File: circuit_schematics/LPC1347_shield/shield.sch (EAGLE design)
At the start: 1 part, among them IC1 7805TV

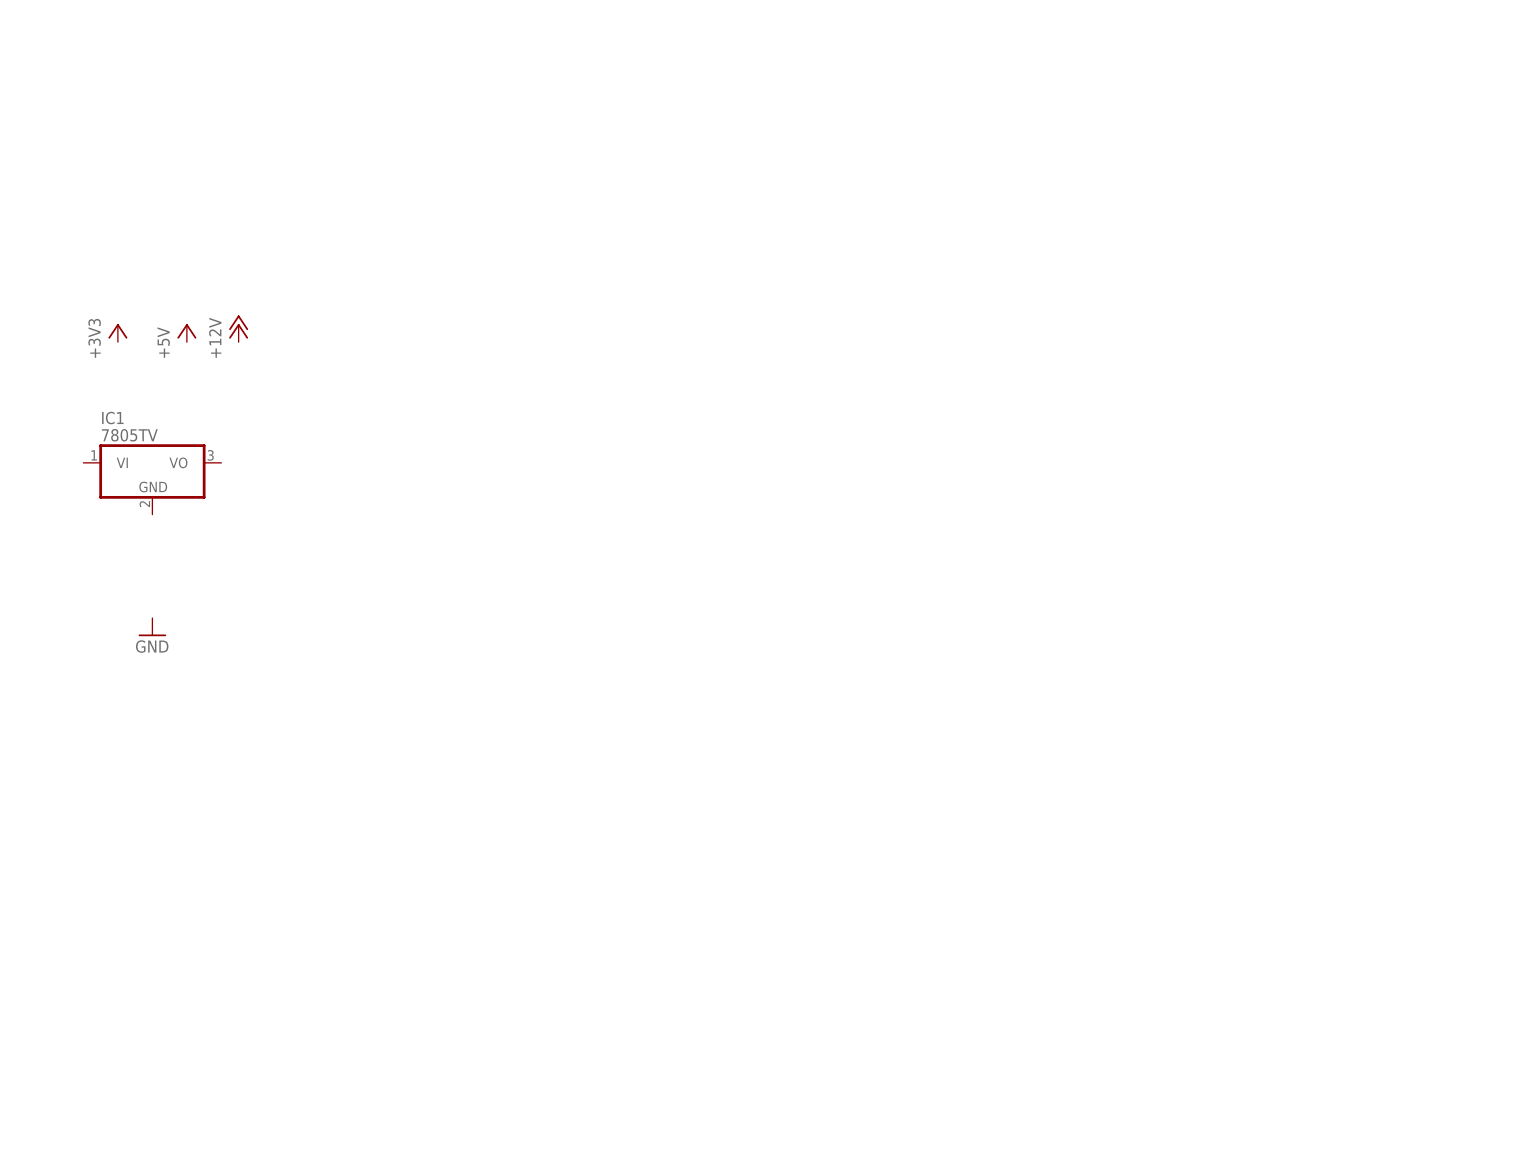
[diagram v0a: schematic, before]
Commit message: Finished circuit board with all traces on top layer.
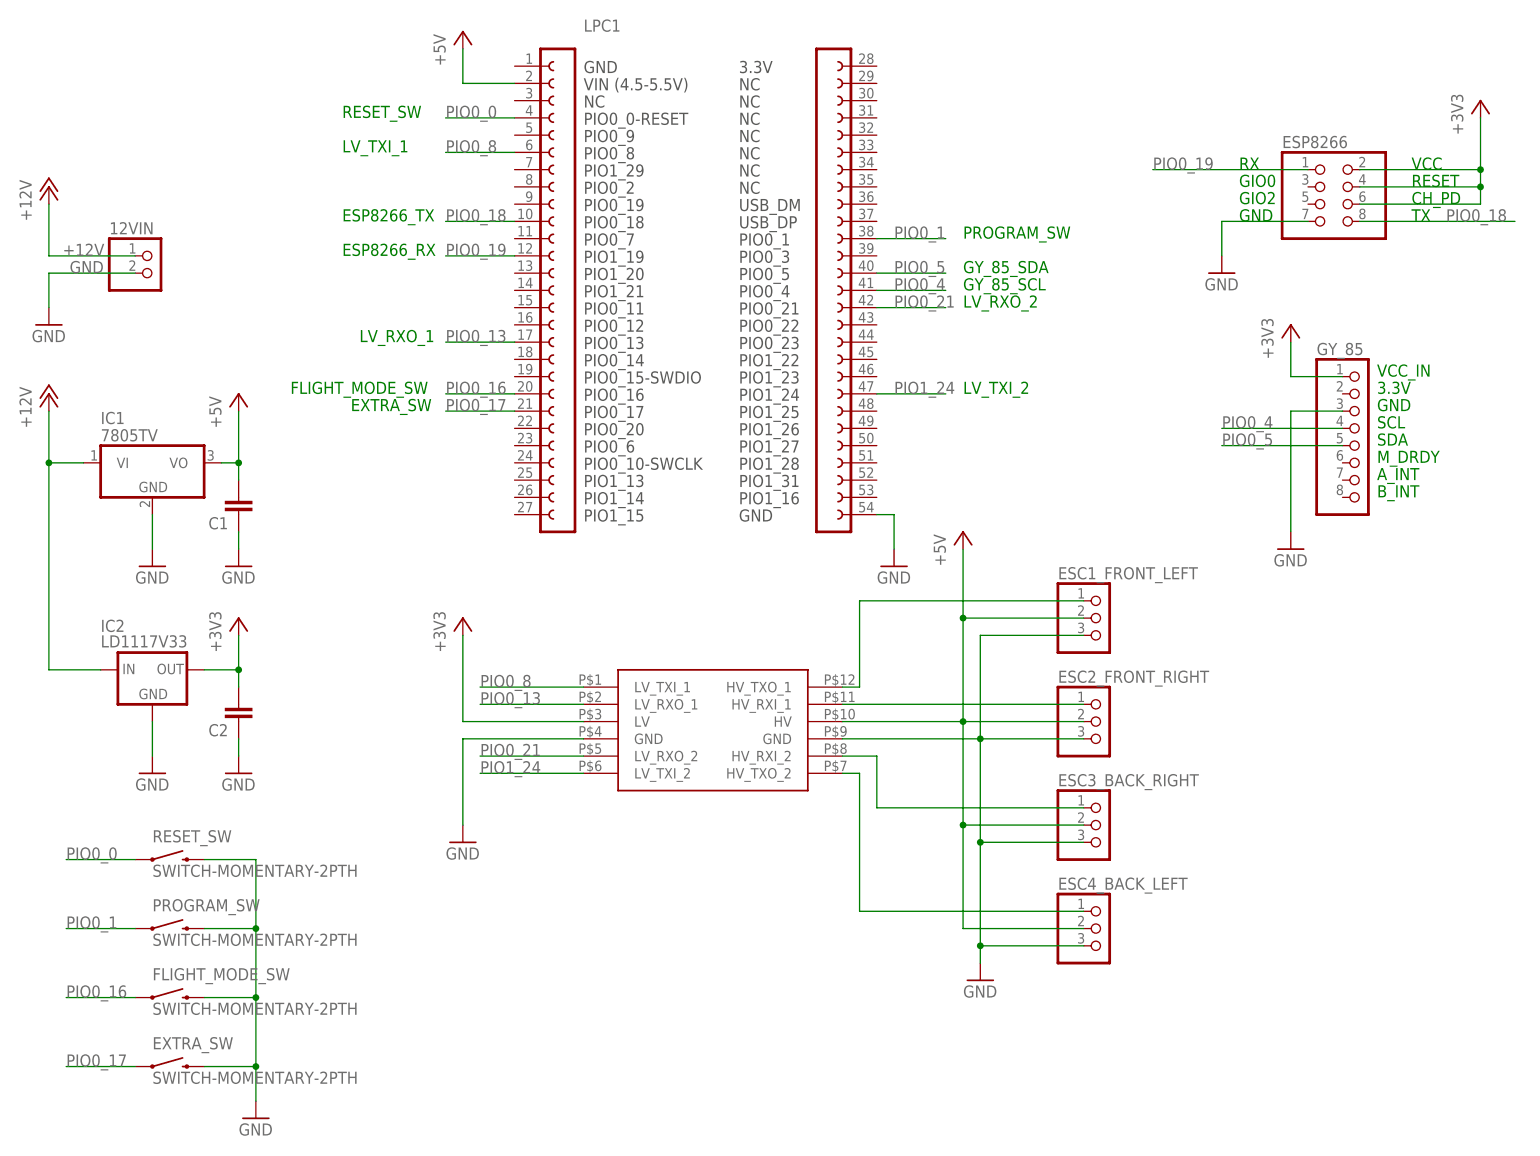
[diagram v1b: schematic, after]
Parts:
- added 12VIN: (no value), pinhead:PINHD-1X2
- added C1, C2: (no value), rcl:C-EU025-024X044
- added ESC1_FRONT_LEFT, ESC2_FRONT_RIGHT, ESC3_BACK_RIGHT, ESC4_BACK_LEFT: (no value), pinhead:PINHD-1X3
- added ESP8266: (no value), pinhead:PINHD-2X4
- added EXTRA_SW, FLIGHT_MODE_SW, PROGRAM_SW, RESET_SW: SWITCH-MOMENTARY-2PTH, SparkFun-Electromechanical:SWITCH-MOMENTARY-2PTH
- added GY_85: (no value), pinhead:PINHD-1X8
- added IC2: LD1117V33, LD1117V33:LD1117V33
- added LPC1: (no value), LPCXpresso_boards:LPCXPRESSO_LPC11U14
- added U$1: LOGIC_LEVEL_CONVERTER, SparkFun-Boards:LOGIC_LEVEL_CONVERTER
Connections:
- new net +12V: 12VIN.1, IC1.VI, IC2.IN
- new net +3V3: C2.2, ESP8266.2, ESP8266.4, ESP8266.6, GY_85.1, IC2.OUT, U$1.LV
- new net +5V: C1.2, ESC1_FRONT_LEFT.2, ESC2_FRONT_RIGHT.2, ESC3_BACK_RIGHT.2, ESC4_BACK_LEFT.2, IC1.VO, LPC1.2, U$1.HV
- new net GND: 12VIN.2, C1.1, C2.1, ESC1_FRONT_LEFT.3, ESC2_FRONT_RIGHT.3, ESC3_BACK_RIGHT.3, ESC4_BACK_LEFT.3, ESP8266.7, EXTRA_SW.2, FLIGHT_MODE_SW.2, GY_85.3, IC1.GND, IC2.GND, LPC1.54, PROGRAM_SW.2, RESET_SW.2, U$1.GND, U$1.GND@2
- new net N$5: ESC4_BACK_LEFT.1, U$1.HV_TXO_2
- new net N$7: ESC3_BACK_RIGHT.1, U$1.HV_RXI_2
- new net N$8: ESC2_FRONT_RIGHT.1, U$1.HV_RXI_1
- new net N$9: ESC1_FRONT_LEFT.1, U$1.HV_TXO_1
- new net PIO0_0: LPC1.4, RESET_SW.1
- new net PIO0_1: LPC1.38, PROGRAM_SW.1
- new net PIO0_13: LPC1.17, U$1.LV_RXO_1
- new net PIO0_16: FLIGHT_MODE_SW.1, LPC1.20
- new net PIO0_17: EXTRA_SW.1, LPC1.21
- new net PIO0_18: ESP8266.8, LPC1.10
- new net PIO0_19: ESP8266.1, LPC1.12
- new net PIO0_21: LPC1.42, U$1.LV_RXO_2
- new net PIO0_4: GY_85.4, LPC1.41
- new net PIO0_5: GY_85.5, LPC1.40
- new net PIO0_8: LPC1.6, U$1.LV_TXI_1
- new net PIO1_24: LPC1.47, U$1.LV_TXI_2
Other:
- note added: "3.3V"
- note added: "A_INT"
- note added: "B_INT"
- note added: "CH_PD"
- note added: "ESP8266_RX"
- note added: "ESP8266_TX"
- note added: "EXTRA_SW"
- note added: "FLIGHT_MODE_SW"
- note added: "GIO0"
- note added: "GIO2"
- note added: "GND"
- note added: "GY_85_SCL"
- note added: "GY_85_SDA"
- note added: "LV_RXO_1"
- note added: "LV_RXO_2"
- note added: "LV_TXI_1"
- note added: "LV_TXI_2"
- note added: "M_DRDY"
- note added: "PROGRAM_SW"
- note added: "RESET"
- note added: "RESET_SW"
- note added: "RX"
- note added: "SCL"
- note added: "SDA"
- note added: "TX"
- note added: "VCC"
- note added: "VCC_IN"

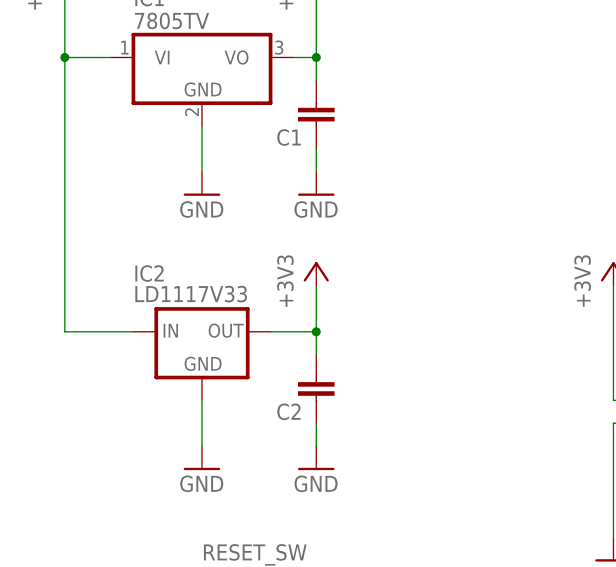
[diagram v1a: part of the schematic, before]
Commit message: Moved all traces to back and fixed all errors.
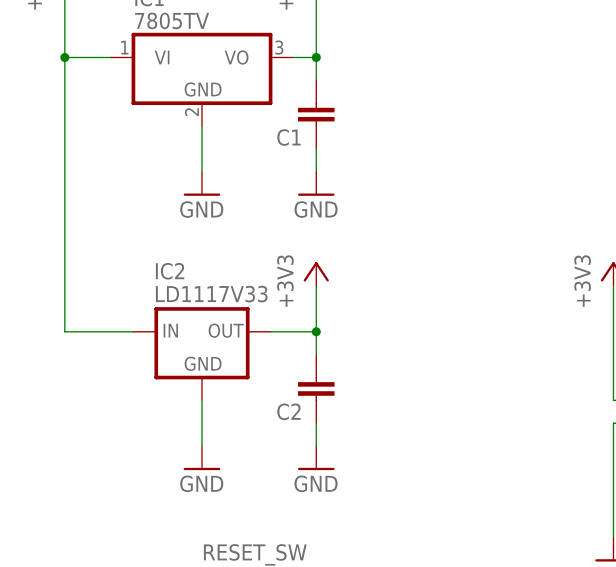
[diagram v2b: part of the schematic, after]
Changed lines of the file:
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@@
 <part name="GND1" library="supply1" deviceset="GND" device=""/>
 <part name="IC1" library="linear" deviceset="78*" device="TV" technology="05"/>
-<part name="IC2" library="LD1117V33" deviceset="LD1117V33" device=""/>
 <part name="GND2" library="supply1" deviceset="GND" device=""/>
 <part name="12VIN" library="pinhead" deviceset="PINHD-1X2" device=""/>
@@
 <part name="GND8" library="supply1" deviceset="GND" device=""/>
 <part name="GND11" library="supply1" deviceset="GND" device=""/>
+<part name="IC2" library="LD1117V33" deviceset="LD1117V33" device=""/>
 </parts>
 <sheets>
@@
 <instance part="GND1" gate="1" x="38.1" y="71.12"/>
 <instance part="IC1" gate="A1" x="38.1" y="116.84"/>
-<instance part="IC2" gate="G$1" x="38.1" y="83.82" smashed="yes">
-<attribute name="NAME" x="30.48" y="91.948" size="1.778" layer="95"/>
-<attribute name="VALUE" x="30.48" y="89.662" size="1.778" layer="96"/>
-</instance>
 <instance part="GND2" gate="1" x="38.1" y="101.6"/>
 <instance part="12VIN" gate="G$1" x="38.1" y="144.78"/>
@@
 <instance part="GND8" gate="1" x="195.58" y="144.78"/>
 <instance part="GND11" gate="1" x="205.74" y="104.14"/>
+<instance part="IC2" gate="G$1" x="38.1" y="83.82" smashed="yes">
+<attribute name="NAME" x="32.766" y="92.202" size="1.778" layer="95"/>
+<attribute name="VALUE" x="32.766" y="89.662" size="1.778" layer="96"/>
+</instance>
 </instances>
 <busses>
@@
 <pinref part="IC1" gate="A1" pin="VI"/>
 <wire x1="22.86" y1="116.84" x2="27.94" y2="116.84" width="0.1524" layer="91"/>
-<pinref part="IC2" gate="G$1" pin="IN"/>
 <wire x1="30.48" y1="86.36" x2="22.86" y2="86.36" width="0.1524" layer="91"/>
 <wire x1="22.86" y1="86.36" x2="22.86" y2="116.84" width="0.1524" layer="91"/>
 <junction x="22.86" y="116.84"/>
+<pinref part="IC2" gate="G$1" pin="IN"/>
 </segment>
 <segment>
@@
 </segment>
 <segment>
-<pinref part="IC2" gate="G$1" pin="GND"/>
 <pinref part="GND1" gate="1" pin="GND"/>
 <wire x1="38.1" y1="78.74" x2="38.1" y2="73.66" width="0.1524" layer="91"/>
+<pinref part="IC2" gate="G$1" pin="GND"/>
 </segment>
 <segment>
@@
 <net name="+3V3" class="0">
 <segment>
-<pinref part="IC2" gate="G$1" pin="OUT"/>
 <pinref part="+3V1" gate="G$1" pin="+3V3"/>
 <wire x1="45.72" y1="86.36" x2="50.8" y2="86.36" width="0.1524" layer="91"/>
@@
 <wire x1="50.8" y1="86.36" x2="50.8" y2="83.82" width="0.1524" layer="91"/>
 <junction x="50.8" y="86.36"/>
-</segment>
-<segment>
+<pinref part="IC2" gate="G$1" pin="OUT"/>
+</segment>
+<segment>
